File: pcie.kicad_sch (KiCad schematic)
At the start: 28 parts, among them J9 1-2199230-6, U1 MIMX8MM6DVTLZAA, U32 SI52112-B5-GM2, U33 74LVC2G07, Y4 25MHz

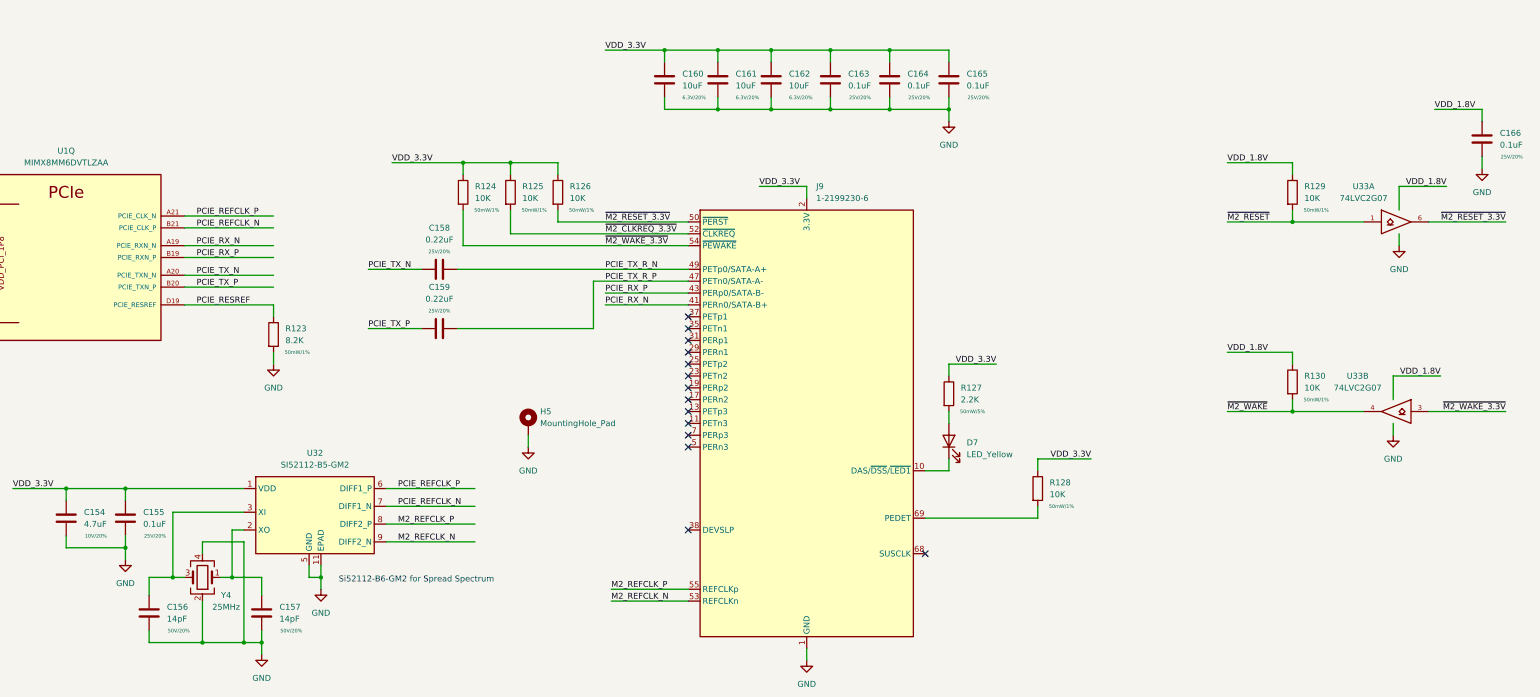
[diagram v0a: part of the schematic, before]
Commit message: inital routing of ddr data bus, sch work
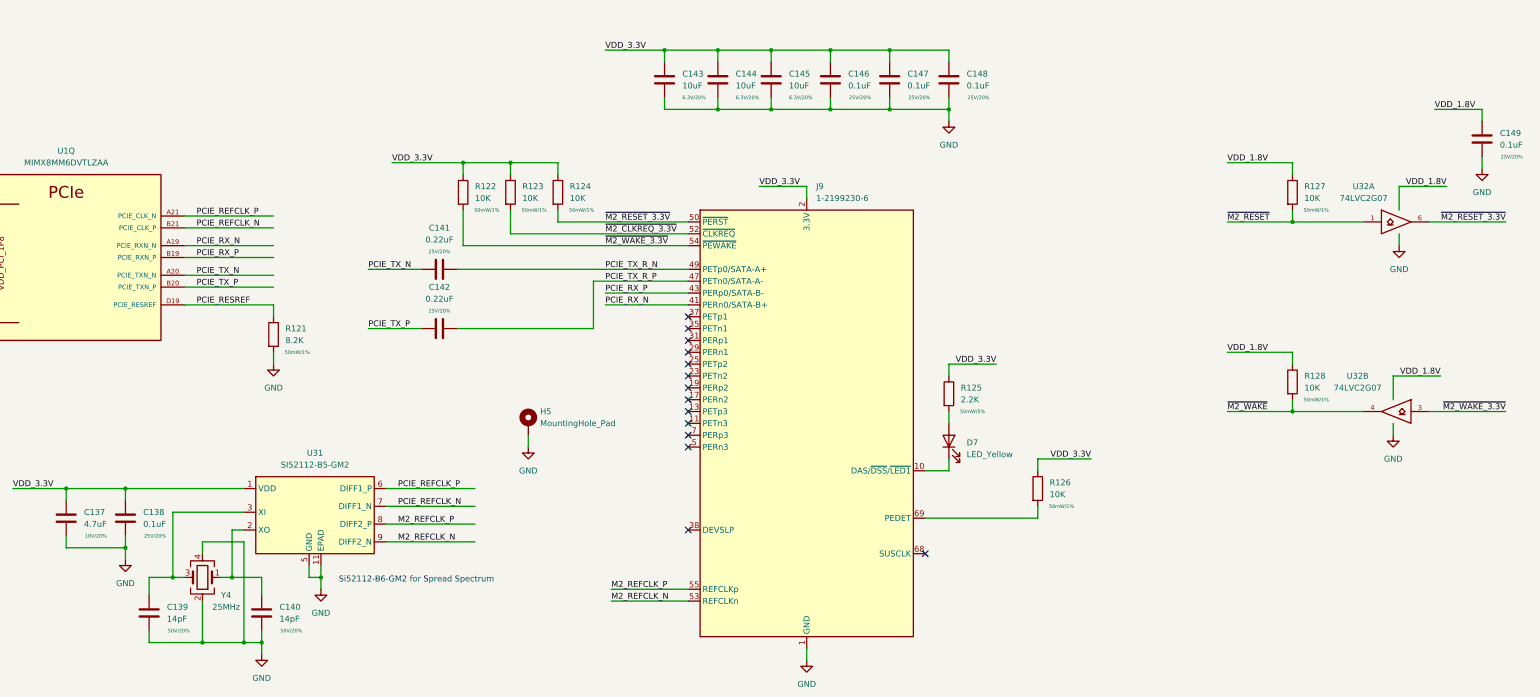
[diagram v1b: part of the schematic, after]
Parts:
- renumbered C154 to C137, C155 to C138, C156 to C139, C157 to C140, C158 to C141, C159 to C142, C160 to C143, C161 to C144, C162 to C145, C163 to C146, C164 to C147, C165 to C148, C166 to C149, R123 to R121, R124 to R122, R125 to R123, R126 to R124, R127 to R125, R128 to R126, R129 to R127, R130 to R128, U32 to U31, U33 to U32

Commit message: add SN65DSI86 DSI2DP ic, SCH, PCB work, flytime work
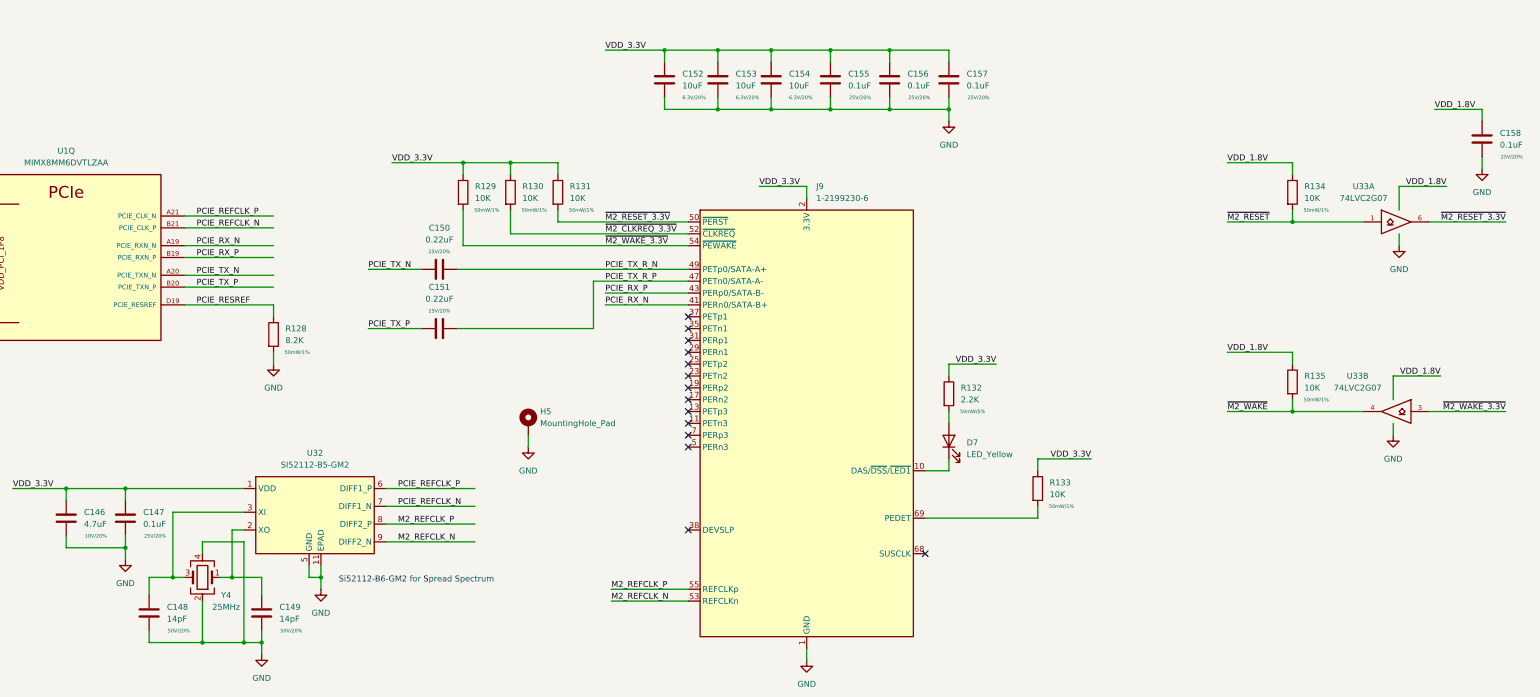
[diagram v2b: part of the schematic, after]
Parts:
- renumbered C137 to C146, C138 to C147, C139 to C148, C140 to C149, C141 to C150, C142 to C151, C143 to C152, C144 to C153, C145 to C154, C146 to C155, C147 to C156, C148 to C157, C149 to C158, R121 to R128, R122 to R129, R123 to R130, R124 to R131, R125 to R132, R126 to R133, R127 to R134, R128 to R135, U31 to U32, U32 to U33

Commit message: add UART4 connector
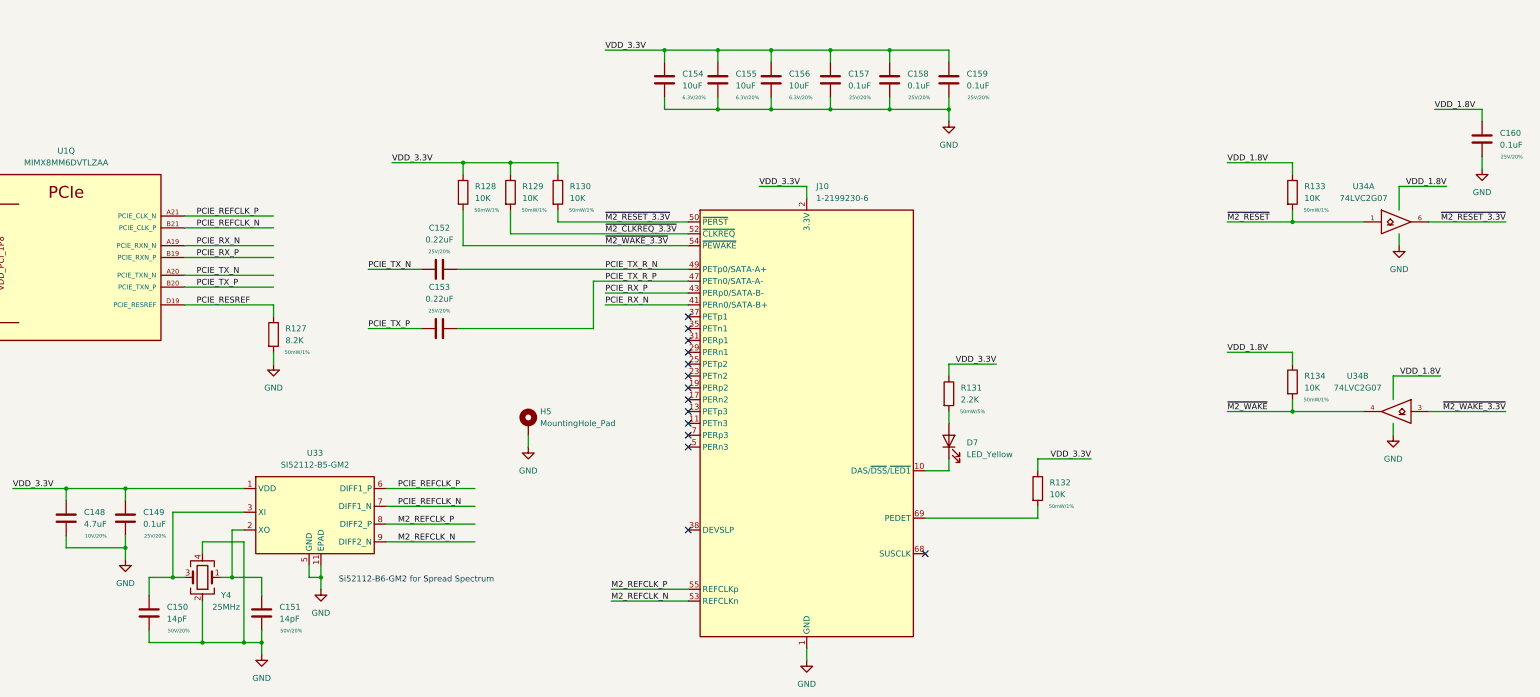
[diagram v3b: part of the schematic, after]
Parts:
- renumbered C146 to C148, C147 to C149, C148 to C150, C149 to C151, C150 to C152, C151 to C153, C152 to C154, C153 to C155, C154 to C156, C155 to C157, C156 to C158, C157 to C159, C158 to C160, J9 to J10, R128 to R127, R129 to R128, R130 to R129, R131 to R130, R132 to R131, R133 to R132, R134 to R133, R135 to R134, U32 to U33, U33 to U34

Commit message: change USB-UART conn, add new 0402 fp, more pcb work
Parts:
- C148, C149, C150, C151, C154, C155, C156, C157, C158, C159, C160: footprint Capacitor_SMD:C_0402_1005Metric -> qsbc:C_0402_1005Metric
- R127, R128, R129, R130, R131, R132, R133, R134: footprint Resistor_SMD:R_0402_1005Metric -> qsbc:R_0402_1005Metric
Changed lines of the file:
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@@
       (effects (font (size 1.27 1.27)) (justify left))
     )
-    (property "Footprint" "Capacitor_SMD:C_0402_1005Metric" (id 2) (at 381.9652 46.99 0)
+    (property "Footprint" "qsbc:C_0402_1005Metric" (id 2) (at 381.9652 46.99 0)
       (effects (font (size 1.27 1.27)) hide)
     )
@@
       (effects (font (size 1.27 1.27)) (justify left))
     )
-    (property "Footprint" "Capacitor_SMD:C_0402_1005Metric" (id 2) (at 254.9652 34.29 0)
+    (property "Footprint" "qsbc:C_0402_1005Metric" (id 2) (at 254.9652 34.29 0)
       (effects (font (size 1.27 1.27)) hide)
     )
@@
       (effects (font (size 1.27 1.27)) (justify left))
     )
-    (property "Footprint" "Resistor_SMD:R_0402_1005Metric" (id 2) (at 264.922 97.79 90)
+    (property "Footprint" "qsbc:R_0402_1005Metric" (id 2) (at 264.922 97.79 90)
       (effects (font (size 1.27 1.27)) hide)
     )
@@
       (effects (font (size 1.27 1.27)) (justify left))
     )
-    (property "Footprint" "Capacitor_SMD:C_0402_1005Metric" (id 2) (at 267.6652 34.29 0)
+    (property "Footprint" "qsbc:C_0402_1005Metric" (id 2) (at 267.6652 34.29 0)
       (effects (font (size 1.27 1.27)) hide)
     )
@@
       (effects (font (size 1.27 1.27)) (justify left))
     )
-    (property "Footprint" "Capacitor_SMD:C_0402_1005Metric" (id 2) (at 229.5652 34.29 0)
+    (property "Footprint" "qsbc:C_0402_1005Metric" (id 2) (at 229.5652 34.29 0)
       (effects (font (size 1.27 1.27)) hide)
     )
@@
       (effects (font (size 1.27 1.27)) (justify left))
     )
-    (property "Footprint" "Resistor_SMD:R_0402_1005Metric" (id 2) (at 120.142 85.09 90)
+    (property "Footprint" "qsbc:R_0402_1005Metric" (id 2) (at 120.142 85.09 90)
       (effects (font (size 1.27 1.27)) hide)
     )
@@
       (effects (font (size 1.27 1.27)) (justify left))
     )
-    (property "Footprint" "Capacitor_SMD:C_0402_1005Metric" (id 2) (at 242.2652 34.29 0)
+    (property "Footprint" "qsbc:C_0402_1005Metric" (id 2) (at 242.2652 34.29 0)
       (effects (font (size 1.27 1.27)) hide)
     )
@@
       (effects (font (size 1.27 1.27)) (justify left))
     )
-    (property "Footprint" "Capacitor_SMD:C_0402_1005Metric" (id 2) (at 91.1352 128.27 0)
+    (property "Footprint" "qsbc:C_0402_1005Metric" (id 2) (at 91.1352 128.27 0)
       (effects (font (size 1.27 1.27)) hide)
     )
@@
       (effects (font (size 1.27 1.27)) (justify left))
     )
-    (property "Footprint" "Resistor_SMD:R_0402_1005Metric" (id 2) (at 338.582 54.61 90)
+    (property "Footprint" "qsbc:R_0402_1005Metric" (id 2) (at 338.582 54.61 90)
       (effects (font (size 1.27 1.27)) hide)
     )
@@
       (effects (font (size 1.27 1.27)) (justify left))
     )
-    (property "Footprint" "Capacitor_SMD:C_0402_1005Metric" (id 2) (at 96.2152 148.59 0)
+    (property "Footprint" "qsbc:C_0402_1005Metric" (id 2) (at 96.2152 148.59 0)
       (effects (font (size 1.27 1.27)) hide)
     )
@@
       (effects (font (size 1.27 1.27)) (justify left))
     )
-    (property "Footprint" "Resistor_SMD:R_0402_1005Metric" (id 2) (at 170.942 54.61 90)
+    (property "Footprint" "qsbc:R_0402_1005Metric" (id 2) (at 170.942 54.61 90)
       (effects (font (size 1.27 1.27)) hide)
     )
@@
       (effects (font (size 1.27 1.27)) (justify left))
     )
-    (property "Footprint" "Resistor_SMD:R_0402_1005Metric" (id 2) (at 283.972 118.11 90)
+    (property "Footprint" "qsbc:R_0402_1005Metric" (id 2) (at 283.972 118.11 90)
       (effects (font (size 1.27 1.27)) hide)
     )
@@
       (effects (font (size 1.27 1.27)) (justify left))
     )
-    (property "Footprint" "Resistor_SMD:R_0402_1005Metric" (id 2) (at 181.102 54.61 90)
+    (property "Footprint" "qsbc:R_0402_1005Metric" (id 2) (at 181.102 54.61 90)
       (effects (font (size 1.27 1.27)) hide)
     )
@@
       (effects (font (size 1.27 1.27)) (justify left))
     )
-    (property "Footprint" "Capacitor_SMD:C_0402_1005Metric" (id 2) (at 120.3452 148.59 0)
+    (property "Footprint" "qsbc:C_0402_1005Metric" (id 2) (at 120.3452 148.59 0)
       (effects (font (size 1.27 1.27)) hide)
     )
@@
       (effects (font (size 1.27 1.27)) (justify left))
     )
-    (property "Footprint" "Capacitor_SMD:C_0402_1005Metric" (id 2) (at 78.4352 128.27 0)
+    (property "Footprint" "qsbc:C_0402_1005Metric" (id 2) (at 78.4352 128.27 0)
       (effects (font (size 1.27 1.27)) hide)
     )
@@
       (effects (font (size 1.27 1.27)) (justify left))
     )
-    (property "Footprint" "Resistor_SMD:R_0402_1005Metric" (id 2) (at 160.782 54.61 90)
+    (property "Footprint" "qsbc:R_0402_1005Metric" (id 2) (at 160.782 54.61 90)
       (effects (font (size 1.27 1.27)) hide)
     )
@@
       (effects (font (size 1.27 1.27)) (justify left))
     )
-    (property "Footprint" "Capacitor_SMD:C_0402_1005Metric" (id 2) (at 218.1352 34.29 0)
+    (property "Footprint" "qsbc:C_0402_1005Metric" (id 2) (at 218.1352 34.29 0)
       (effects (font (size 1.27 1.27)) hide)
     )
@@
       (effects (font (size 1.27 1.27)) (justify left))
     )
-    (property "Footprint" "Capacitor_SMD:C_0402_1005Metric" (id 2) (at 206.7052 34.29 0)
+    (property "Footprint" "qsbc:C_0402_1005Metric" (id 2) (at 206.7052 34.29 0)
       (effects (font (size 1.27 1.27)) hide)
     )
@@
       (effects (font (size 1.27 1.27)) (justify left))
     )
-    (property "Footprint" "Resistor_SMD:R_0402_1005Metric" (id 2) (at 338.582 95.25 90)
-      (effects (font (size 1.27 1.27)) hide)
-    )
+    (property "Footprint" "qsbc:R_0402_1005Metric" (id 2) (at 338.582 95.25 90)
+      (effects (font (size 1.27 1.27)) hide)
+    )

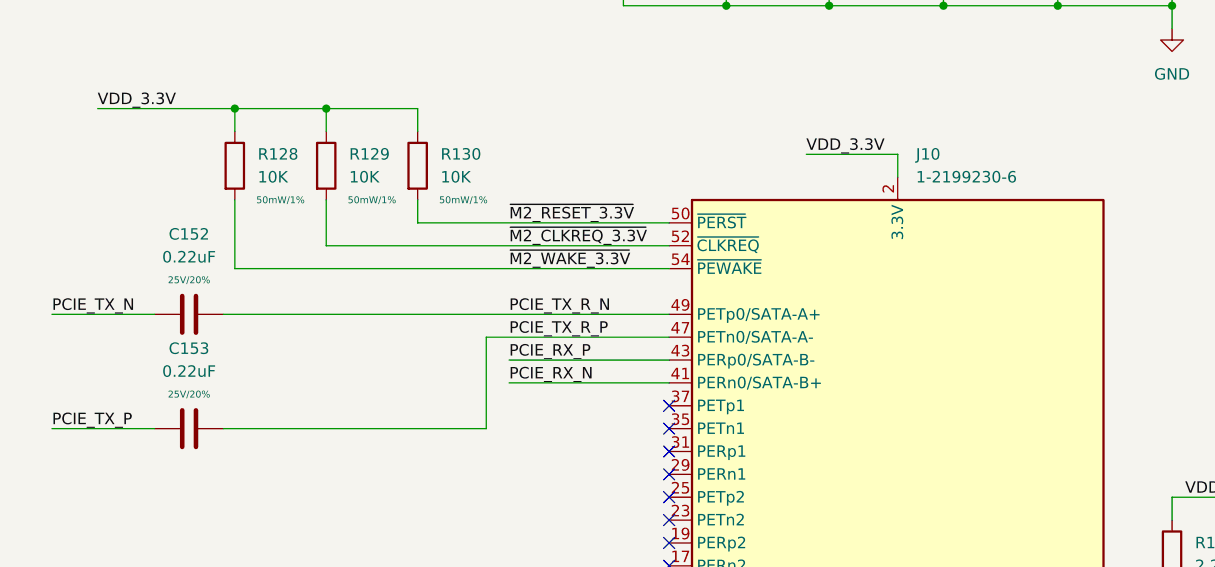
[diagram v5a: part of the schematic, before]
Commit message: bom work, change uart level shifter and m.2 socket
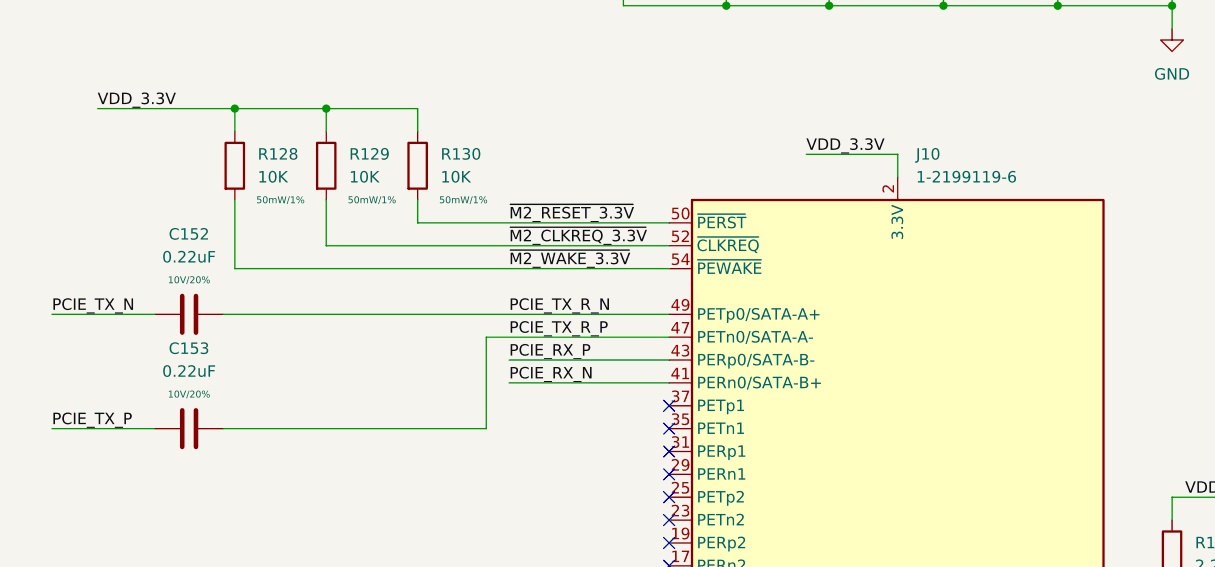
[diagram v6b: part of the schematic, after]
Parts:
- C148: MPN (none) -> CL05A475MP5NRNC
- C149, C157, C158, C159, C160: MPN (none) -> CL05A104KA5NNNC
- C150, C151: MPN (none) -> 04025U140FAT2A
- C152, C153: MPN (none) -> GRM033R61A224KE90D; Rating 25V/20% -> 10V/20%
- C154, C155, C156: MPN (none) -> GRM155R60J106ME44D
- D7: MPN (none) -> SML-E12Y8WT86
- H5: footprint Mounting_Wuerth:Mounting_Wuerth_WA-SMSI-M3_H2.5mm_9774025360 -> Mounting_Wuerth:Mounting_Wuerth_WA-SMSI-M2_H1.5mm_9774015243; MPN (none) -> 9774015243R
- J10: value 1-2199230-6 -> 1-2199119-6; MPN (none) -> 1-2199119-6
- R127: MPN (none) -> RC0402FR-078K2L
- R128, R129, R130, R132, R133, R134: MPN (none) -> RC0402FR-0710KL
- R131: MPN (none) -> RC0402FR-072K2L
- U1: MPN (none) -> MIMX8MM6DVTLZAA
- U33: MPN (none) -> SI52112-B5-GM2
- U34: MPN (none) -> 74LVC2G07FZ4-7
